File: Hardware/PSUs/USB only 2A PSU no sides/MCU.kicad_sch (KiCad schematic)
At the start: 14 parts, among them J12 USB, U4 CH32X035G8U6, U5 THVD1420DRLR

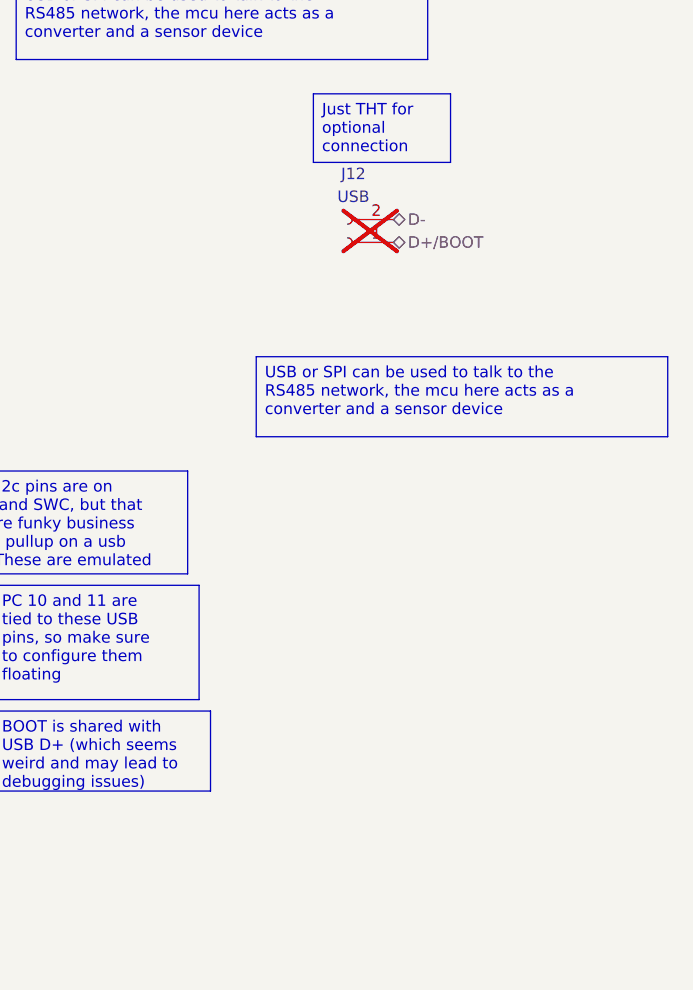
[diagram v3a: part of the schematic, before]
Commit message: Added USB bus and finished preliminary routing
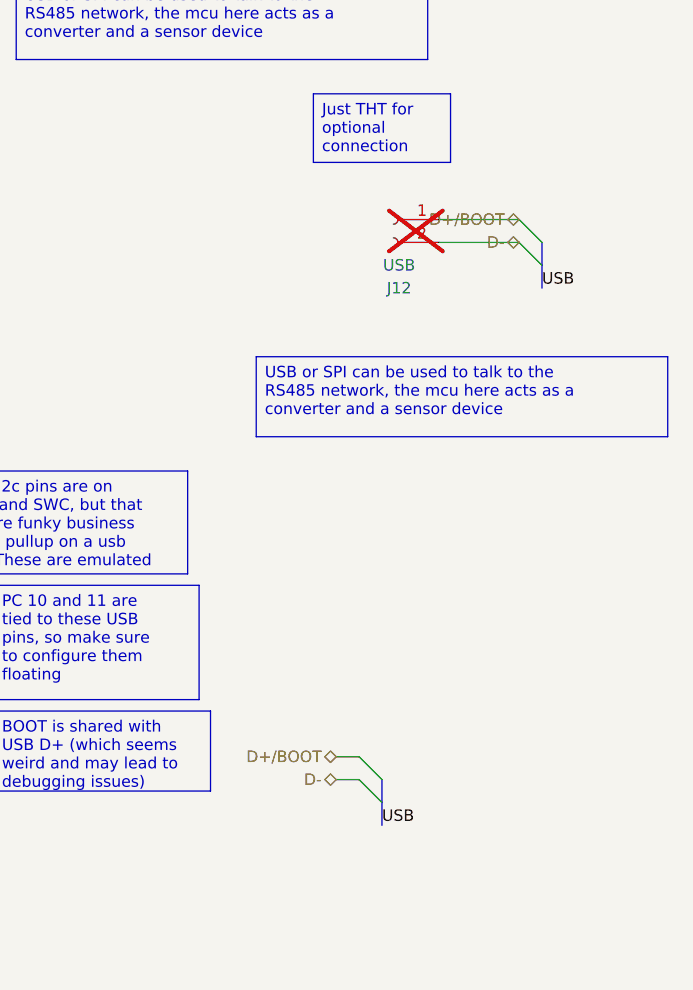
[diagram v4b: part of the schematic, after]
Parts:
- U4: footprint Package_DFN_QFN:QFN-28-1EP_4x4mm_P0.4mm_EP2.4x2.4mm -> qfn_custom:QFN-28-1EP_4x4mm_P0.4mm_EP2.8x2.8mm
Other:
- moved on the sheet: J12
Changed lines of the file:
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@@
 		(at 142.24 85.09)
 	)
+	(bus_entry
+		(at 238.76 121.92)
+		(size 2.54 2.54)
+		(stroke
+			(width 0)
+			(type default)
+		)
+	)
+	(bus_entry
+		(at 256.54 64.77)
+		(size 2.54 2.54)
+		(stroke
+			(width 0)
+			(type default)
+		)
+	)
+	(bus_entry
+		(at 238.76 124.46)
+		(size 2.54 2.54)
+		(stroke
+			(width 0)
+			(type default)
+		)
+	)
+	(bus_entry
+		(at 256.54 62.23)
+		(size 2.54 2.54)
+		(stroke
+			(width 0)
+			(type default)
+		)
+	)
 	(polyline
 		(pts
@@
 		)
 	)
+	(bus
+		(pts
+			(xy 259.08 64.77) (xy 259.08 67.31)
+		)
+		(stroke
+			(width 0)
+			(type default)
+		)
+	)
+	(wire
+		(pts
+			(xy 236.22 124.46) (xy 238.76 124.46)
+		)
+		(stroke
+			(width 0)
+			(type default)
+		)
+	)
 	(wire
 		(pts
@@
 		)
 	)
+	(bus
+		(pts
+			(xy 259.08 67.31) (xy 259.08 69.85)
+		)
+		(stroke
+			(width 0)
+			(type default)
+		)
+	)
 	(wire
 		(pts
@@
 		)
 	)
+	(bus
+		(pts
+			(xy 241.3 124.46) (xy 241.3 127)
+		)
+		(stroke
+			(width 0)
+			(type default)
+		)
+	)
 	(wire
 		(pts
@@
 		)
 	)
+	(bus
+		(pts
+			(xy 241.3 127) (xy 241.3 129.54)
+		)
+		(stroke
+			(width 0)
+			(type default)
+		)
+	)
+	(wire
+		(pts
+			(xy 236.22 121.92) (xy 238.76 121.92)
+		)
+		(stroke
+			(width 0)
+			(type default)
+		)
+	)
+	(wire
+		(pts
+			(xy 247.65 62.23) (xy 256.54 62.23)
+		)
+		(stroke
+			(width 0)
+			(type default)
+		)
+	)
 	(wire
 		(pts
@@
 	(wire
 		(pts
+			(xy 247.65 64.77) (xy 256.54 64.77)
+		)
+		(stroke
+			(width 0)
+			(type default)
+		)
+	)
+	(wire
+		(pts
 			(xy 74.93 147.32) (xy 68.58 147.32)
 		)
@@
 			(width 0)
 			(type default)
+		)
+	)
+	(label "USB"
+		(at 241.3 129.54 0)
+		(effects
+			(font
+				(size 1.27 1.27)
+			)
+			(justify left bottom)
 		)
 	)
@@
 	(label "UART1_TX"
 		(at 177.8 90.17 0)
+		(effects
+			(font
+				(size 1.27 1.27)
+			)
+			(justify left bottom)
+		)
+	)
+	(label "USB"
+		(at 259.08 69.85 0)
 		(effects
 			(font
@@
 		)
 	)
+	(hierarchical_label "D-"
+		(shape bidirectional)
+		(at 236.22 124.46 180)
+		(effects
+			(font
+				(size 1.27 1.27)
+			)
+			(justify right)
+		)
+	)
 	(hierarchical_label "SDA"
 		(shape output)
@@
 		)
 	)
+	(hierarchical_label "D-"
+		(shape bidirectional)
+		(at 256.54 64.77 180)
+		(effects
+			(font
+				(size 1.27 1.27)
+			)
+			(justify right)
+		)
+	)
 	(hierarchical_label "SDA"
 		(shape output)
@@
 			)
 			(justify left)
+		)
+	)
+	(hierarchical_label "D+{slash}BOOT"
+		(shape bidirectional)
+		(at 256.54 62.23 180)
+		(effects
+			(font
+				(size 1.27 1.27)
+			)
+			(justify right)
 		)
 	)
@@
 	(hierarchical_label "D+{slash}BOOT"
 		(shape bidirectional)
-		(at 242.57 64.77 0)
-		(effects
-			(font
-				(size 1.27 1.27)
-			)
-			(justify left)
+		(at 236.22 121.92 180)
+		(effects
+			(font
+				(size 1.27 1.27)
+			)
+			(justify right)
 		)
 	)
@@
 			)
 			(justify right)
-		)
-	)
-	(hierarchical_label "D-"
-		(shape bidirectional)
-		(at 242.57 62.23 0)
-		(effects
-			(font
-				(size 1.27 1.27)
-			)
-			(justify left)
 		)
 	)
@@
 			)
 		)
-		(property "Footprint" "Package_DFN_QFN:QFN-28-1EP_4x4mm_P0.4mm_EP2.4x2.4mm"
+		(property "Footprint" "qfn_custom:QFN-28-1EP_4x4mm_P0.4mm_EP2.8x2.8mm"
 			(at 165.1 153.67 0)
 			(effects
@@
 	(symbol
 		(lib_id "Connector:Conn_01x02_Socket")
-		(at 237.49 64.77 180)
+		(at 242.57 62.23 0)
+		(mirror y)
 		(unit 1)
 		(exclude_from_sim no)
@@
 		(fields_autoplaced yes)
 		(property "Reference" "J12"
-			(at 238.125 57.15 0)
+			(at 243.205 69.85 0)
 			(effects
 				(font
@@
 		)
 		(property "Value" "USB"
-			(at 238.125 59.69 0)
+			(at 243.205 67.31 0)
 			(effects
 				(font
@@
 		)
 		(property "Footprint" "Connector_PinHeader_1.27mm:PinHeader_1x02_P1.27mm_Vertical"
-			(at 237.49 64.77 0)
+			(at 242.57 62.23 0)
 			(effects
 				(font
@@
 		)
 		(property "Datasheet" "~"
-			(at 237.49 64.77 0)
+			(at 242.57 62.23 0)
 			(effects
 				(font
@@
 		)
 		(property "Description" "Generic connector, single row, 01x02, script generated"
-			(at 237.49 64.77 0)
-			(effects
-				(font
+			(at 242.57 62.23 0)
+			(effects
+				(font
